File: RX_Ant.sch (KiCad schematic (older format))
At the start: 36 parts, among them J1 CONN_COAXIAL, J10 CONN_COAXIAL, J11 CONN_01X06, J12 CONN_01X05, J13 CONN_COAXIAL, J14 CONN_COAXIAL, J2 CONN_COAXIAL, J3 CONN_COAXIAL, J4 CONN_COAXIAL, J5 CONN_COAXIAL, J6 CONN_COAXIAL, J7 CONN_COAXIAL, J8 CONN_COAXIAL, J9 CONN_COAXIAL

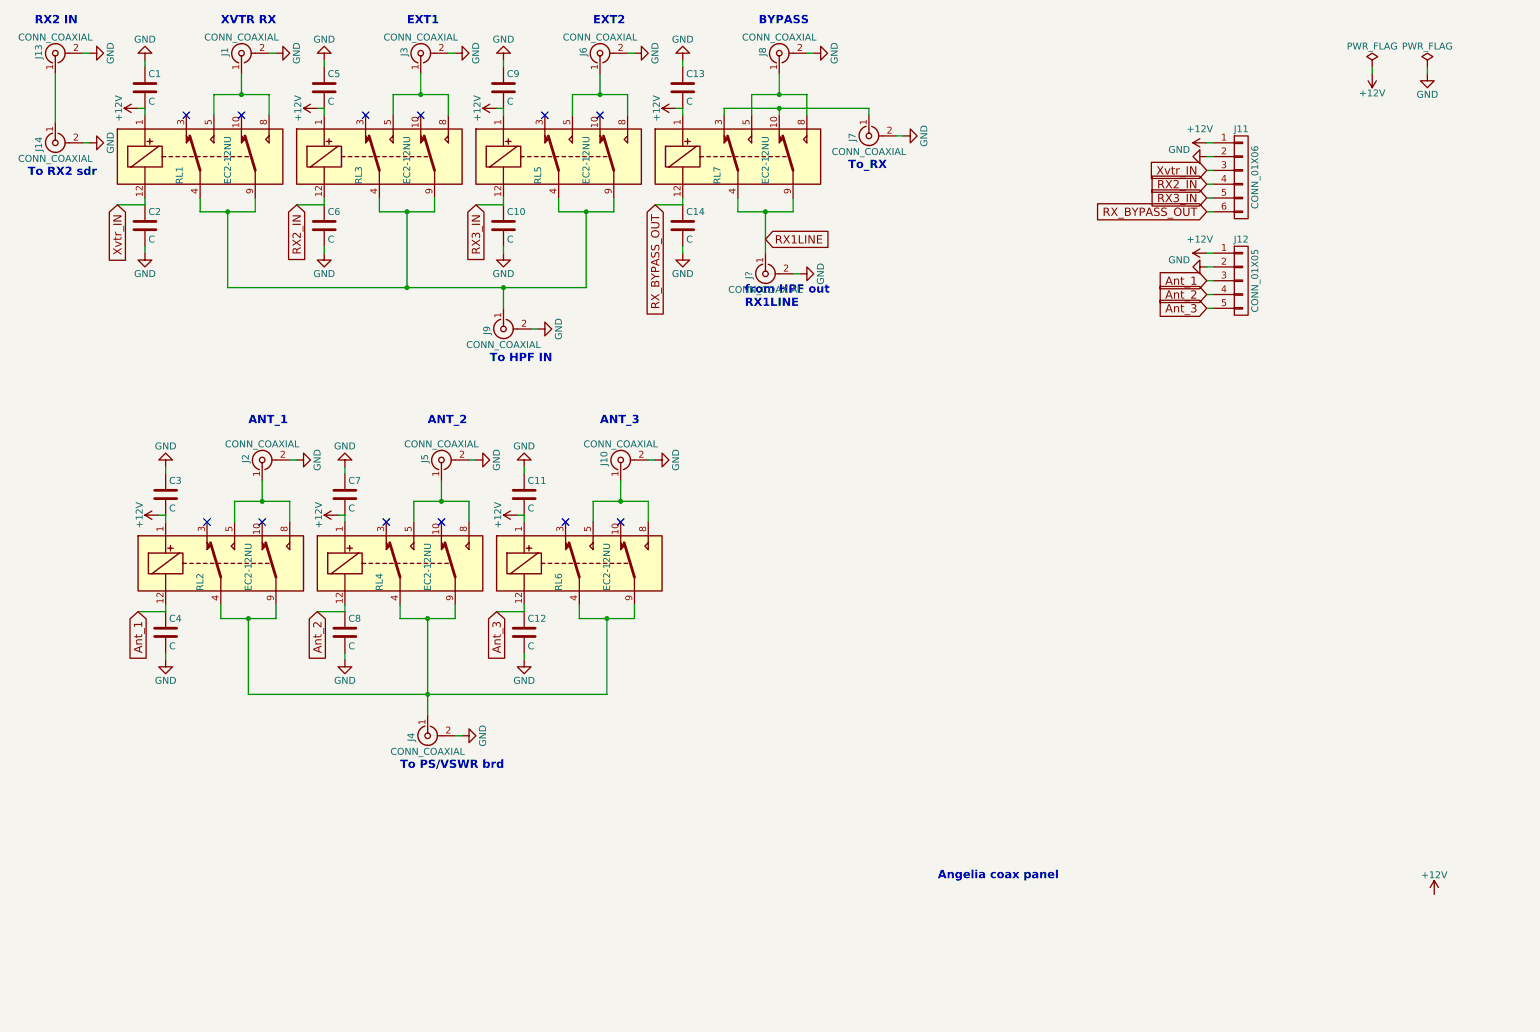
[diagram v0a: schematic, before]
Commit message: adding sma and relay modules
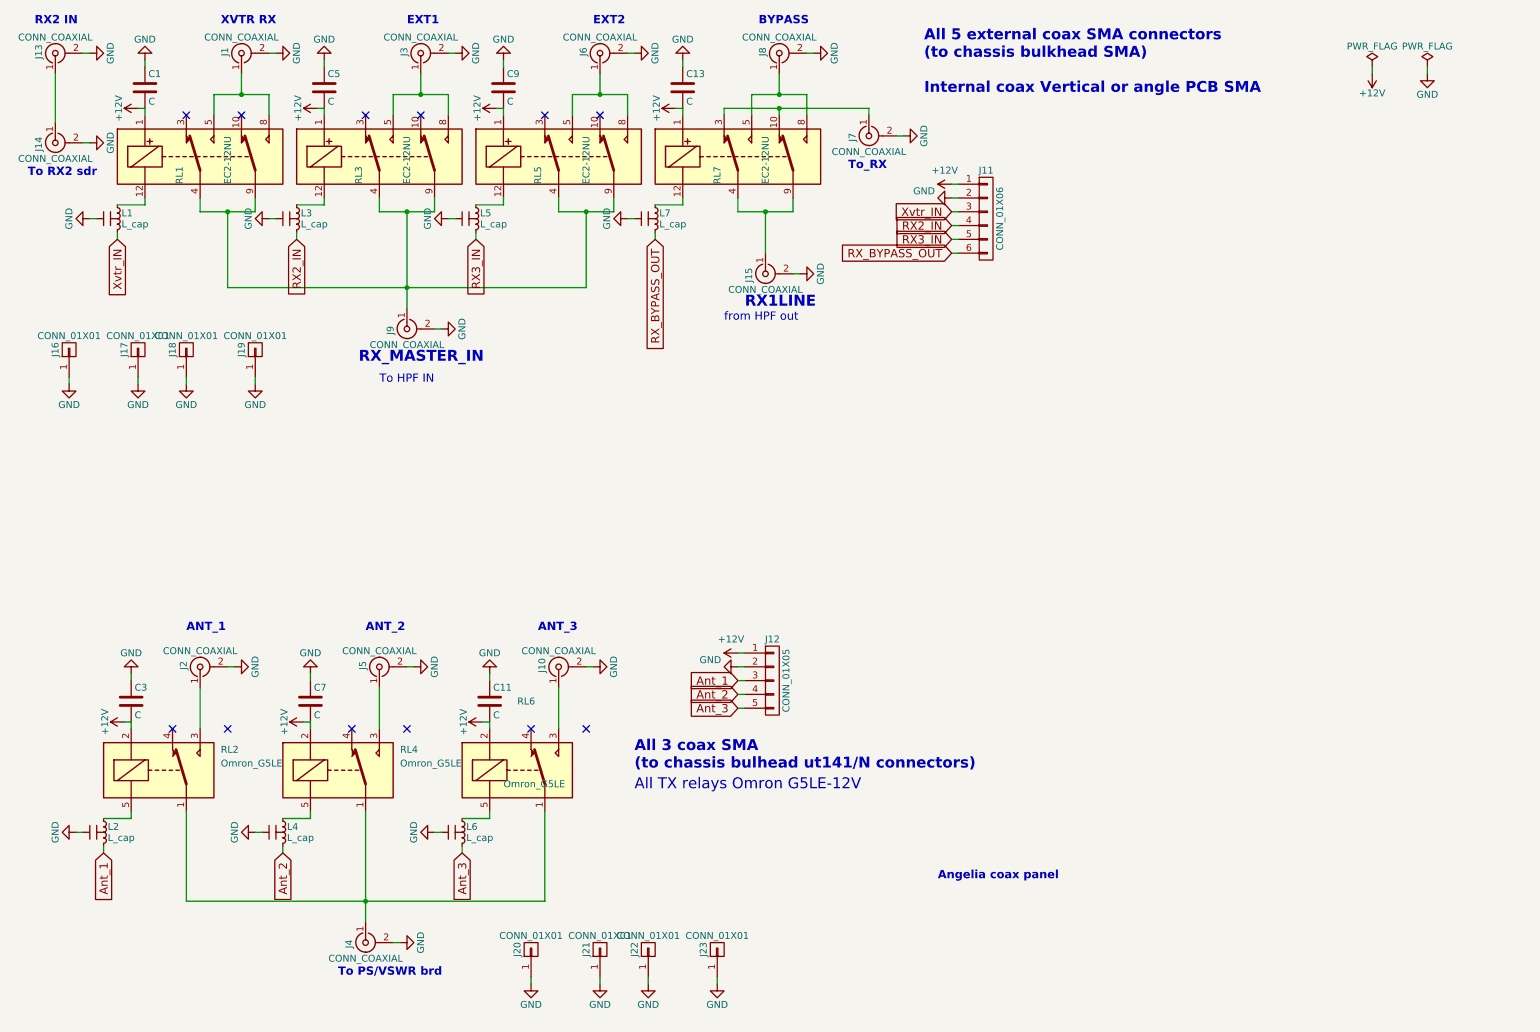
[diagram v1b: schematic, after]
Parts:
- removed C10, C12, C14, C2, C4, C6, C8: C, Capacitors_SMD:C_0805_HandSoldering, symbol C
- removed RL2, RL4, RL6: EC2-12NU, 2_Form_C_Relay:THT_2_formC, symbol EC2-12NU
- added J16, J17, J18, J19, J20, J21, J22, J23: CONN_01X01, Mounting_Holes:MountingHole_3.5mm_Pad, symbol CONN_01X01
- added L1, L2, L3, L4, L5, L6, L7: L_cap, Ferrite_LC_NFM41P:Ferrite_LC_NFM41P, symbol L_cap
- added RL2, RL4, RL6: Omron_G5LE, Omron_G5LE:Omron_G5LE, symbol Omron_G5LE
- J1, J10, J13, J14, J2, J3, J4, J5, J6, J7, J8, J9: footprint SMA_PINS:SMA_PINS -> conn_rf:sma_straight_32k101-400l5
- J15: renamed from J?; footprint SMA_PINS:SMA_PINS -> conn_rf:sma_straight_32k101-400l5
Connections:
- net +12V: now also RL2.2, RL4.2, RL6.2
- net Ant_1: now also L2.3
- net Ant_2: now also L4.3
- net Ant_3: now also L6.3
- net GND: now also J16.1 (P1), J17.1 (P1), J18.1 (P1), J19.1 (P1), J20.1 (P1), J21.1 (P1), J22.1 (P1), J23.1 (P1), L1.2, L2.2, L3.2, L4.2, L5.2, L6.2, L7.2
- net RX2_IN: now also L3.3; no longer RL3.12
- net RX3_IN: now also L5.3; no longer RL5.12
- net RX_BYPASS_OUT: now also L7.3; no longer RL7.12
- net Xvtr_IN: now also L1.3; no longer RL1.12
- net at J2.1 (In): now also RL2.3
- net at J4.1 (In): now also RL2.1, RL4.1, RL6.1
- net at J5.1 (In): now also RL4.3
- net at J10.1 (In): now also RL6.3
- net RX1LINE: no longer names the net of J15.1 (In), RL7.4, RL7.9
- new net: L1.1, RL1.12
- new net: L3.1, RL3.12
- new net: L5.1, RL5.12
- new net: L7.1, RL7.12
- new net: L6.1, RL6.5
- new net: L2.1, RL2.5
- new net: L4.1, RL4.5
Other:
- note added: "All 3 coax SMA\n(to chassis bulhead ut141/N connectors)"
- note added: "All 5 external coax SMA connectors\n(to chassis bulkhead SMA)\n\nInternal coax Vertical or angle PCB SMA"
- note added: "All TX relays Omron G5LE-12V"
- note added: "RX_MASTER_IN"
- note added: "\nRX1LINE"
- note added: "from HPF out"
- note removed: "from HPF out\nRX1LINE"
- moved on the sheet: C11, C3, C7, J10, J11, J12, J2, J4, J5, J9

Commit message: Readme cleaning, add 2 3D pictures
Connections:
- no-connect marks 12 -> 9
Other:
- note added: "All 5 external coax SMA connectors\n(to chassis bulkhead SMA or N)\n\nInternal coax Vertical or angle PCB SMA"
- note removed: "All 5 external coax SMA connectors\n(to chassis bulkhead SMA)\n\nInternal coax Vertical or angle PCB SMA"
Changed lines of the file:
@@
 	1750 5400 1750 5700
 NoConn ~ 1550 5700
-NoConn ~ 1950 5700
 Wire Wire Line
 	1650 6300 1650 6950
@@
 	3050 5400 3050 5700
 NoConn ~ 2850 5700
-NoConn ~ 3250 5700
 Wire Wire Line
 	2950 6300 2950 7100
@@
 	4350 5400 4350 5700
 NoConn ~ 4150 5700
-NoConn ~ 4550 5700
 Wire Wire Line
 	4250 6950 4250 6300
@@
 All 3 coax SMA\n(to chassis bulhead ut141/N connectors)
 Text Notes 7000 1100 0    79   ~ 16
-All 5 external coax SMA connectors\n(to chassis bulkhead SMA)\n\nInternal coax Vertical or angle PCB SMA
+All 5 external coax SMA connectors\n(to chassis bulkhead SMA or N)\n\nInternal coax Vertical or angle PCB SMA
 $Comp
 L L_cap L6

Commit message: Gerber and BOM files added
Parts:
- added J24, J25, J26, J27, J28, J29, J30, J31, J32, J33, J34, J35, J36: CONN_COAXIAL, Connector_Coaxial:SMA_Amphenol_132289_EdgeMount, symbol CONN_COAXIAL
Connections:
- net GND: now also J24.2 (Ext), J25.2 (Ext), J26.2 (Ext), J27.2 (Ext), J28.2 (Ext), J29.2 (Ext), J30.2 (Ext), J31.2 (Ext), J32.2 (Ext), J33.2 (Ext), J34.2 (Ext), J35.2 (Ext), J36.2 (Ext)
- net at J1.1 (In), RL1.5, RL1.8: now also J26.1 (In)
- net at J9.1 (In), RL1.4, RL1.9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: now also J28.1 (In)
- net at J3.1 (In), RL3.5, RL3.8: now also J29.1 (In)
- net at J6.1 (In), RL5.5, RL5.8: now also J31.1 (In)
- net at J8.1 (In), RL7.5, RL7.8: now also J32.1 (In)
- net at J7.1 (In), RL7.10, RL7.3: now also J36.1 (In)
- net at J15.1 (In), RL7.4, RL7.9: now also J35.1 (In)
- net at J2.1 (In), RL2.3: now also J25.1 (In)
- net at J5.1 (In), RL4.3: now also J27.1 (In)
- net at J4.1 (In), RL2.1, RL4.1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: now also J34.1 (In)
- net at J10.1 (In), RL6.3: now also J30.1 (In)
- net at J13.1 (In), J14.1 (In): now also J24.1 (In), J33.1 (In)
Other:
- moved on the sheet: C1, C13, C5, C9, J1, J11, J13, J14, J15, J16, J17, J18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

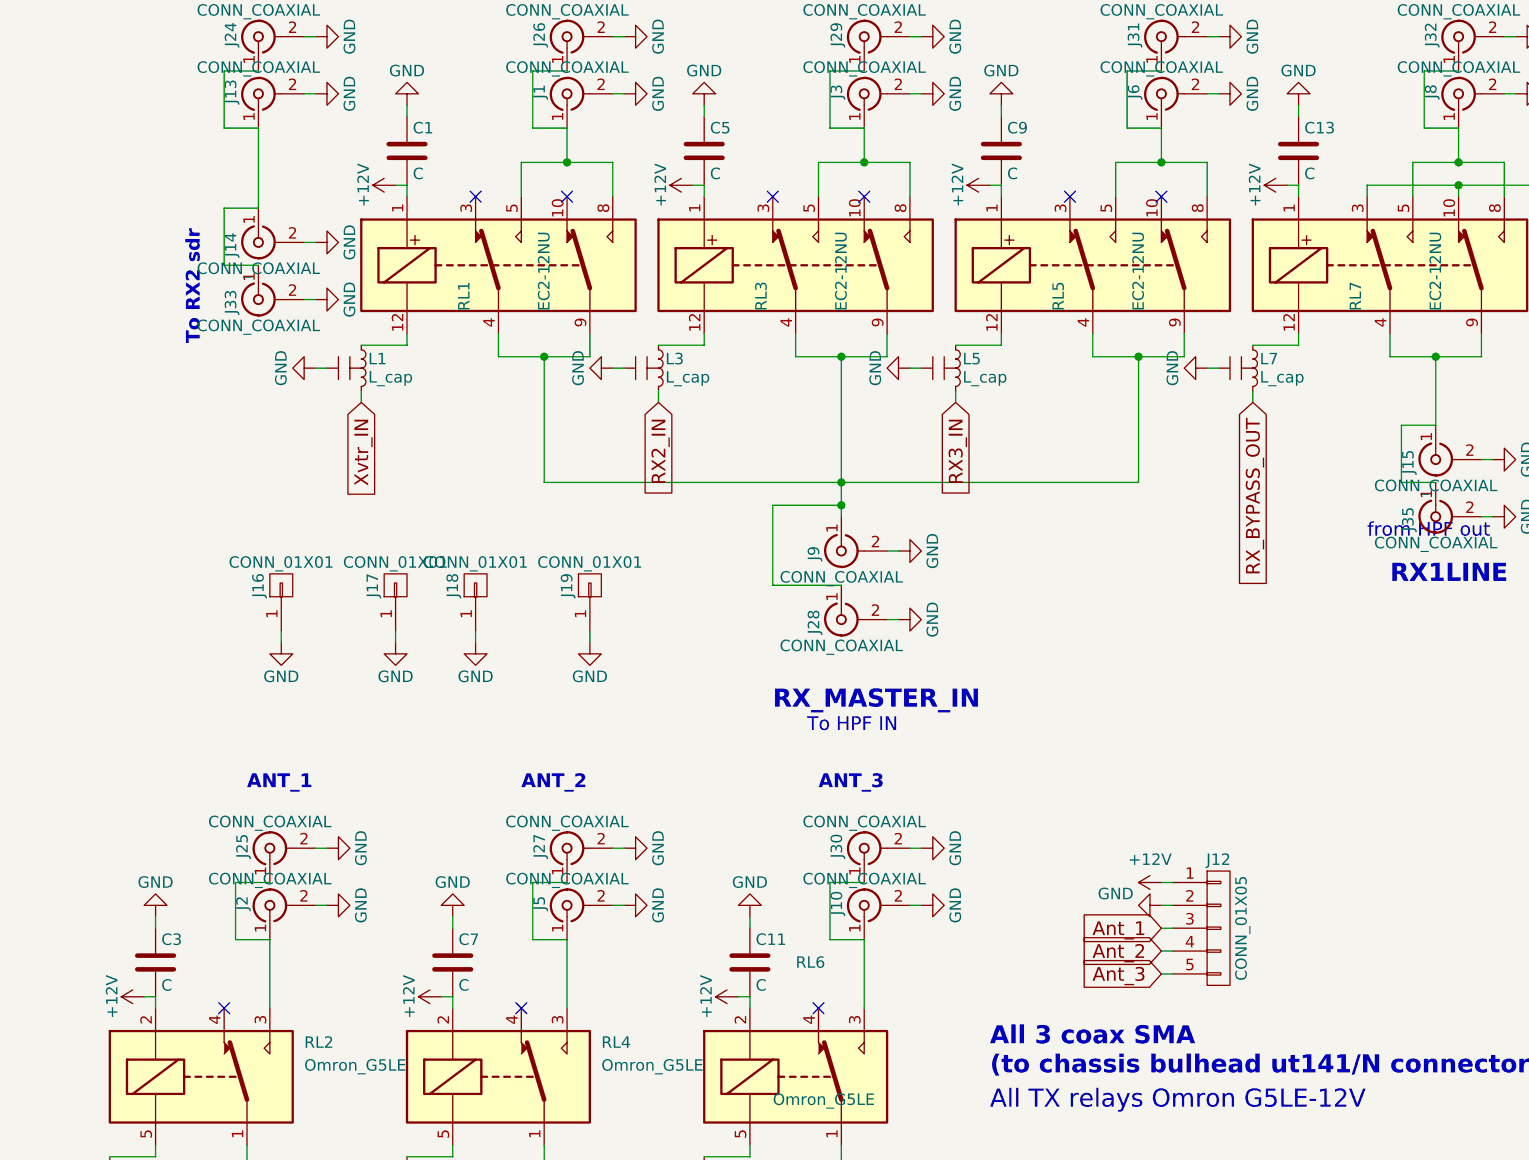
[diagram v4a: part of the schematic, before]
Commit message: component values added, BOM changed
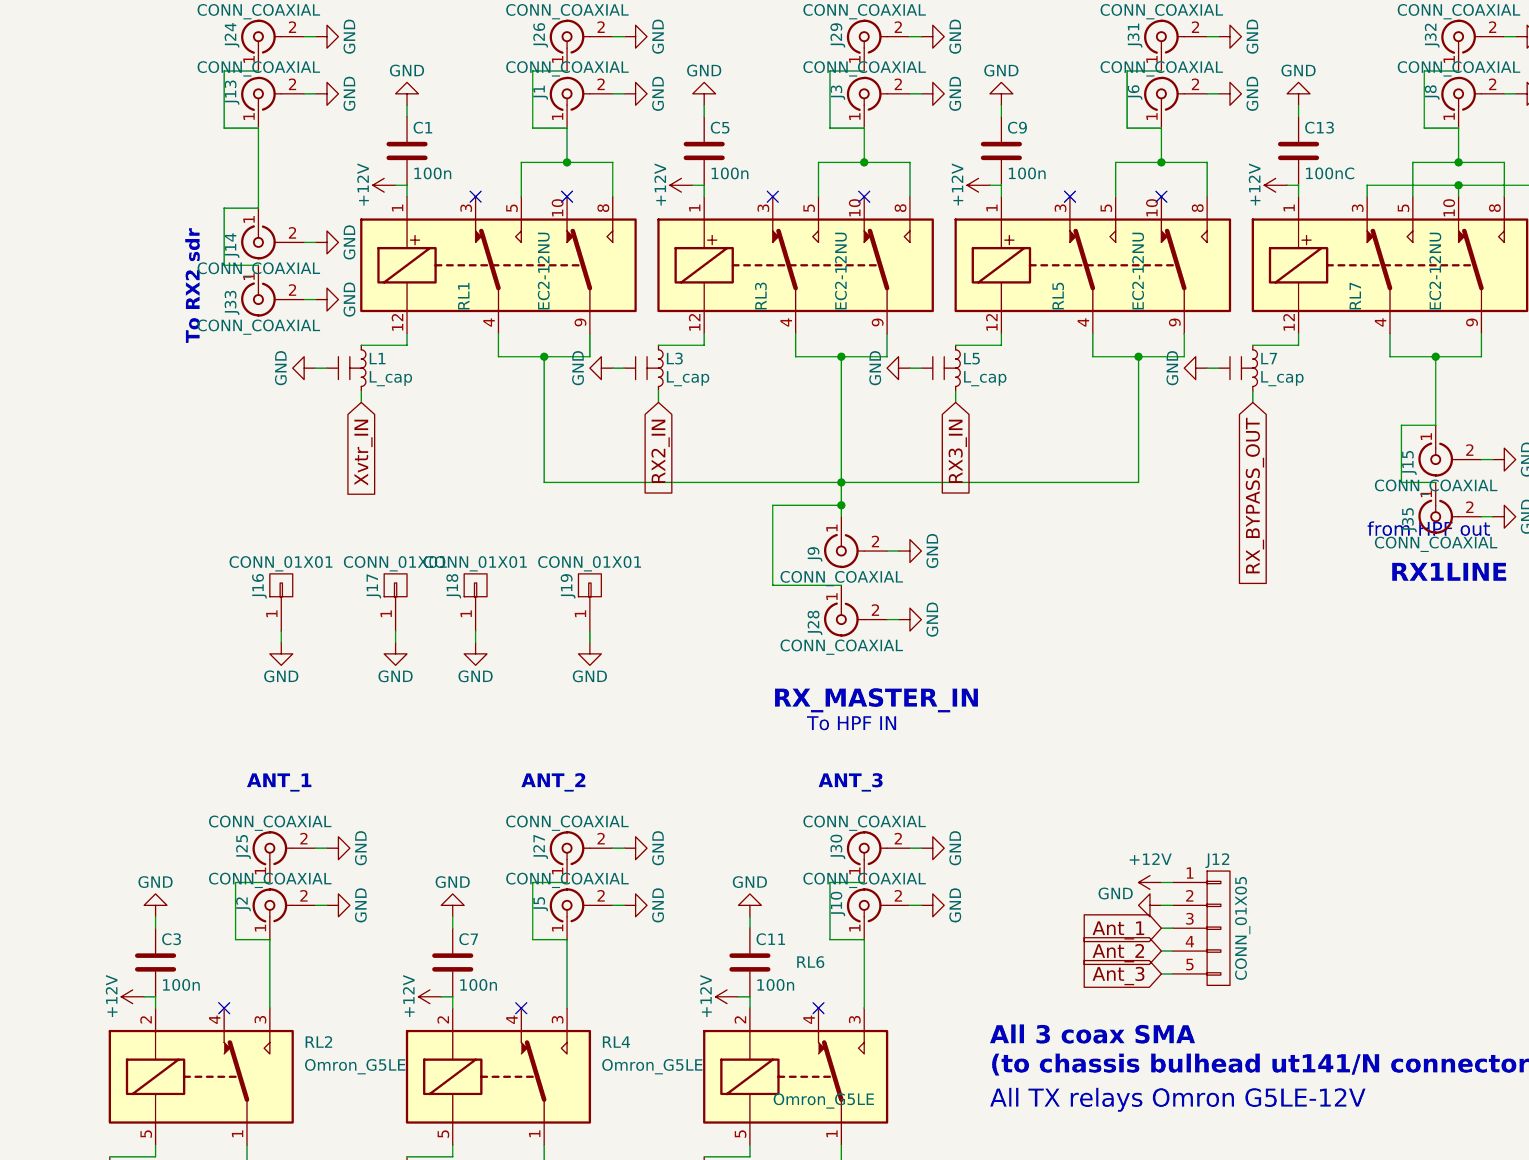
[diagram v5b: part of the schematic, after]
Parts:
- C1, C11, C3, C5, C7, C9: value C -> 100n
- C13: value C -> 100nC
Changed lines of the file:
@@
 P 2350 1950
 F 0 "C1" H 2375 2050 50  0000 L CNN
-F 1 "C" H 2375 1850 50  0000 L CNN
+F 1 "100n" H 2375 1850 50  0000 L CNN
 F 2 "Capacitors_SMD:C_0805_HandSoldering" H 2388 1800 50  0001 C CNN
 F 3 "" H 2350 1950 50  0001 C CNN
@@
 P 3650 1950
 F 0 "C5" H 3675 2050 50  0000 L CNN
-F 1 "C" H 3675 1850 50  0000 L CNN
+F 1 "100n" H 3675 1850 50  0000 L CNN
 F 2 "Capacitors_SMD:C_0805_HandSoldering" H 3688 1800 50  0001 C CNN
 F 3 "" H 3650 1950 50  0001 C CNN
@@
 P 4950 1950
 F 0 "C9" H 4975 2050 50  0000 L CNN
-F 1 "C" H 4975 1850 50  0000 L CNN
+F 1 "100n" H 4975 1850 50  0000 L CNN
 F 2 "Capacitors_SMD:C_0805_HandSoldering" H 4988 1800 50  0001 C CNN
 F 3 "" H 4950 1950 50  0001 C CNN
@@
 P 6250 1950
 F 0 "C13" H 6275 2050 50  0000 L CNN
-F 1 "C" H 6275 1850 50  0000 L CNN
+F 1 "100nC" H 6275 1850 50  0000 L CNN
 F 2 "Capacitors_SMD:C_0805_HandSoldering" H 6288 1800 50  0001 C CNN
 F 3 "" H 6250 1950 50  0001 C CNN
@@
 P 1250 5500
 F 0 "C3" H 1275 5600 50  0000 L CNN
-F 1 "C" H 1275 5400 50  0000 L CNN
+F 1 "100n" H 1275 5400 50  0000 L CNN
 F 2 "Capacitors_SMD:C_0805_HandSoldering" H 1288 5350 50  0001 C CNN
 F 3 "" H 1250 5500 50  0001 C CNN
@@
 P 2550 5500
 F 0 "C7" H 2575 5600 50  0000 L CNN
-F 1 "C" H 2575 5400 50  0000 L CNN
+F 1 "100n" H 2575 5400 50  0000 L CNN
 F 2 "Capacitors_SMD:C_0805_HandSoldering" H 2588 5350 50  0001 C CNN
 F 3 "" H 2550 5500 50  0001 C CNN
@@
 P 3850 5500
 F 0 "C11" H 3875 5600 50  0000 L CNN
-F 1 "C" H 3875 5400 50  0000 L CNN
+F 1 "100n" H 3875 5400 50  0000 L CNN
 F 2 "Capacitors_SMD:C_0805_HandSoldering" H 3888 5350 50  0001 C CNN
 F 3 "" H 3850 5500 50  0001 C CNN

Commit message: new routing, new gerber
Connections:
- net +12V: now also J11.6 (P6), J12.5 (P5); no longer J11.1 (P1), J12.1 (P1)
- net Ant_2: now also J12.2 (P2); no longer J12.4 (P4)
- net Ant_3: now also J12.1 (P1); no longer J12.5 (P5)
- net GND: now also J11.5 (P5), J12.4 (P4); no longer J11.2 (P2), J12.2 (P2)
- net RX2_IN: now also J11.3 (P3); no longer J11.4 (P4)
- net RX3_IN: now also J11.2 (P2); no longer J11.5 (P5)
- net RX_BYPASS_OUT: now also J11.1 (P1); no longer J11.6 (P6)
- net Xvtr_IN: now also J11.4 (P4); no longer J11.3 (P3)
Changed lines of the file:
@@
 F 3 "" H 5900 5350 50  0001 C CNN
 	1    5900 5350
-	1    0    0    -1
+	1    0    0    1
 $EndComp
 $Comp
@@
 F 3 "" H 8450 2900 50  0001 C CNN
 	1    8450 2900
-	1    0    0    -1
+	1    0    0    1
 $EndComp
 Text GLabel 8200 3150 0    60   Input ~ 0
